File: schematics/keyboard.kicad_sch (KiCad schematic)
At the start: 35 parts

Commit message: cleanup, fixes, started on power supplies
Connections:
- net C6: no longer S?.2, S?.2, S?.2, S?.2
- net KB10: no longer S?.2, S?.2, S?.2, S?.2, S?.2, S?.2, S?.2, S?.2, S?.2
- net KB12: no longer S?.2, S?.2, S?.2, S?.2, S?.2, S?.2, S?.2
- net KB9: no longer S?.2, S?.2, S?.2, S?.2, S?.2, S?.2, S?.2
- no-connect marks 27 -> 54
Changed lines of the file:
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@@
   (no_connect (at 236.22 73.66))
   (no_connect (at 254 53.34))
+  (no_connect (at 149.86 63.5))
+  (no_connect (at 149.86 53.34))
+  (no_connect (at 132.08 53.34))
+  (no_connect (at 132.08 63.5))
+  (no_connect (at 88.9 83.82))
+  (no_connect (at 88.9 53.34))
+  (no_connect (at 88.9 63.5))
+  (no_connect (at 149.86 83.82))
+  (no_connect (at 132.08 83.82))
+  (no_connect (at 109.22 83.82))
+  (no_connect (at 109.22 63.5))
+  (no_connect (at 208.28 83.82))
+  (no_connect (at 172.72 63.5))
+  (no_connect (at 190.5 73.66))
+  (no_connect (at 190.5 63.5))
+  (no_connect (at 172.72 53.34))
+  (no_connect (at 226.06 83.82))
+  (no_connect (at 226.06 63.5))
+  (no_connect (at 226.06 73.66))
+  (no_connect (at 226.06 53.34))
+  (no_connect (at 208.28 73.66))
+  (no_connect (at 208.28 53.34))
+  (no_connect (at 208.28 63.5))
+  (no_connect (at 243.84 63.5))
+  (no_connect (at 243.84 53.34))
+  (no_connect (at 243.84 73.66))
+  (no_connect (at 243.84 83.82))
   (no_connect (at 99.06 83.82))
   (no_connect (at 218.44 63.5))
@@
     (pin "9")
   )
-  (symbol (lib_id "Custom:SW_Push_SPDT") (at 114.3 60.96 0) (unit 1)
+  (symbol (lib_name "SW_Push_SPDT_11") (lib_id "Custom:SW_Push_SPDT") (at 114.3 60.96 0) (unit 1)
     (in_bom yes) (on_board yes)
     (property "Reference" "S?" (id 0) (at 114.3 60.96 0))
@@
     (pin "4")
   )
-  (symbol (lib_id "Custom:SW_Push_SPDT") (at 213.36 71.12 0) (unit 1)
+  (symbol (lib_name "SW_Push_SPDT_26") (lib_id "Custom:SW_Push_SPDT") (at 213.36 71.12 0) (unit 1)
     (in_bom yes) (on_board yes)
     (property "Reference" "S?" (id 0) (at 213.36 71.12 0))
@@
     (pin "2")
   )
-  (symbol (lib_id "Custom:SW_Push_SPDT") (at 248.92 60.96 0) (unit 1)
+  (symbol (lib_name "SW_Push_SPDT_18") (lib_id "Custom:SW_Push_SPDT") (at 248.92 60.96 0) (unit 1)
     (in_bom yes) (on_board yes)
     (property "Reference" "S?" (id 0) (at 248.92 60.96 0))
@@
     (pin "4")
   )
-  (symbol (lib_id "Custom:SW_Push_SPDT") (at 231.14 81.28 0) (unit 1)
+  (symbol (lib_name "SW_Push_SPDT_19") (lib_id "Custom:SW_Push_SPDT") (at 231.14 81.28 0) (unit 1)
     (in_bom yes) (on_board yes)
     (property "Reference" "S?" (id 0) (at 231.14 81.28 0))
@@
     (pin "9")
   )
-  (symbol (lib_id "Custom:SW_Push_SPDT") (at 93.98 81.28 0) (unit 1)
+  (symbol (lib_name "SW_Push_SPDT_8") (lib_id "Custom:SW_Push_SPDT") (at 93.98 81.28 0) (unit 1)
     (in_bom yes) (on_board yes)
     (property "Reference" "S?" (id 0) (at 93.98 81.28 0))
@@
     (pin "4")
   )
-  (symbol (lib_id "Custom:SW_Push_SPDT") (at 231.14 60.96 0) (unit 1)
+  (symbol (lib_name "SW_Push_SPDT_22") (lib_id "Custom:SW_Push_SPDT") (at 231.14 60.96 0) (unit 1)
     (in_bom yes) (on_board yes)
     (property "Reference" "S?" (id 0) (at 231.14 60.96 0))
@@
     (pin "4")
   )
-  (symbol (lib_id "Custom:SW_Push_SPDT") (at 154.94 50.8 0) (unit 1)
+  (symbol (lib_name "SW_Push_SPDT_2") (lib_id "Custom:SW_Push_SPDT") (at 154.94 50.8 0) (unit 1)
     (in_bom yes) (on_board yes)
     (property "Reference" "S?" (id 0) (at 154.94 50.8 0))
@@
     (pin "4")
   )
-  (symbol (lib_id "Custom:SW_Push_SPDT") (at 137.16 60.96 0) (unit 1)
+  (symbol (lib_name "SW_Push_SPDT_4") (lib_id "Custom:SW_Push_SPDT") (at 137.16 60.96 0) (unit 1)
     (in_bom yes) (on_board yes)
     (property "Reference" "S?" (id 0) (at 137.16 60.96 0))
@@
     (pin "4")
   )
-  (symbol (lib_id "Custom:SW_Push_SPDT") (at 137.16 81.28 0) (unit 1)
+  (symbol (lib_name "SW_Push_SPDT_7") (lib_id "Custom:SW_Push_SPDT") (at 137.16 81.28 0) (unit 1)
     (in_bom yes) (on_board yes)
     (property "Reference" "S?" (id 0) (at 137.16 81.28 0))
@@
     (pin "4")
   )
-  (symbol (lib_id "Custom:SW_Push_SPDT") (at 177.8 60.96 0) (unit 1)
+  (symbol (lib_name "SW_Push_SPDT_14") (lib_id "Custom:SW_Push_SPDT") (at 177.8 60.96 0) (unit 1)
     (in_bom yes) (on_board yes)
     (property "Reference" "S?" (id 0) (at 177.8 60.96 0))
@@
     (pin "4")
   )
-  (symbol (lib_id "Custom:SW_Push_SPDT") (at 248.92 71.12 0) (unit 1)
+  (symbol (lib_name "SW_Push_SPDT_20") (lib_id "Custom:SW_Push_SPDT") (at 248.92 71.12 0) (unit 1)
     (in_bom yes) (on_board yes)
     (property "Reference" "S?" (id 0) (at 248.92 71.12 0))
@@
     (pin "4")
   )
-  (symbol (lib_id "Custom:SW_Push_SPDT") (at 231.14 50.8 0) (unit 1)
+  (symbol (lib_name "SW_Push_SPDT_24") (lib_id "Custom:SW_Push_SPDT") (at 231.14 50.8 0) (unit 1)
     (in_bom yes) (on_board yes)
     (property "Reference" "S?" (id 0) (at 231.14 50.8 0))
@@
     (pin "4")
   )
-  (symbol (lib_id "Custom:SW_Push_SPDT") (at 93.98 60.96 0) (unit 1)
+  (symbol (lib_name "SW_Push_SPDT_6") (lib_id "Custom:SW_Push_SPDT") (at 93.98 60.96 0) (unit 1)
     (in_bom yes) (on_board yes)
     (property "Reference" "S?" (id 0) (at 93.98 60.96 0))
@@
     (pin "4")
   )
-  (symbol (lib_id "Custom:SW_Push_SPDT") (at 177.8 50.8 0) (unit 1)
+  (symbol (lib_name "SW_Push_SPDT_16") (lib_id "Custom:SW_Push_SPDT") (at 177.8 50.8 0) (unit 1)
     (in_bom yes) (on_board yes)
     (property "Reference" "S?" (id 0) (at 177.8 50.8 0))
@@
     (pin "4")
   )
-  (symbol (lib_id "Custom:SW_Push_SPDT") (at 154.94 81.28 0) (unit 1)
+  (symbol (lib_name "SW_Push_SPDT_9") (lib_id "Custom:SW_Push_SPDT") (at 154.94 81.28 0) (unit 1)
     (in_bom yes) (on_board yes)
     (property "Reference" "S?" (id 0) (at 154.94 81.28 0))
@@
     (pin "2")
   )
-  (symbol (lib_id "Custom:SW_Push_SPDT") (at 154.94 60.96 0) (unit 1)
+  (symbol (lib_name "SW_Push_SPDT_3") (lib_id "Custom:SW_Push_SPDT") (at 154.94 60.96 0) (unit 1)
     (in_bom yes) (on_board yes)
     (property "Reference" "S?" (id 0) (at 154.94 60.96 0))
@@
     (pin "4")
   )
-  (symbol (lib_id "Custom:SW_Push_SPDT") (at 195.58 71.12 0) (unit 1)
+  (symbol (lib_name "SW_Push_SPDT_13") (lib_id "Custom:SW_Push_SPDT") (at 195.58 71.12 0) (unit 1)
     (in_bom no) (on_board yes)
     (property "Reference" "S?" (id 0) (at 195.58 71.12 0))
@@
     (pin "2")
   )
-  (symbol (lib_id "Custom:SW_Push_SPDT") (at 248.92 81.28 0) (unit 1)
+  (symbol (lib_name "SW_Push_SPDT_21") (lib_id "Custom:SW_Push_SPDT") (at 248.92 81.28 0) (unit 1)
     (in_bom yes) (on_board yes)
     (property "Reference" "S?" (id 0) (at 248.92 81.28 0))
@@
     (pin "4")
   )
-  (symbol (lib_id "Custom:SW_Push_SPDT") (at 93.98 50.8 0) (unit 1)
+  (symbol (lib_name "SW_Push_SPDT_5") (lib_id "Custom:SW_Push_SPDT") (at 93.98 50.8 0) (unit 1)
     (in_bom yes) (on_board yes)
     (property "Reference" "S?" (id 0) (at 93.98 50.8 0))
@@
     (pin "2")
   )
-  (symbol (lib_id "Custom:SW_Push_SPDT") (at 114.3 81.28 0) (unit 1)
+  (symbol (lib_name "SW_Push_SPDT_10") (lib_id "Custom:SW_Push_SPDT") (at 114.3 81.28 0) (unit 1)
     (in_bom yes) (on_board yes)
     (property "Reference" "S?" (id 0) (at 114.3 81.28 0))
@@
     (pin "4")
   )
-  (symbol (lib_id "Custom:SW_Push_SPDT") (at 213.36 60.96 0) (unit 1)
+  (symbol (lib_name "SW_Push_SPDT_25") (lib_id "Custom:SW_Push_SPDT") (at 213.36 60.96 0) (unit 1)
     (in_bom yes) (on_board yes)
     (property "Reference" "S?" (id 0) (at 213.36 60.96 0))
@@
     (pin "4")
   )
-  (symbol (lib_id "Custom:SW_Push_SPDT") (at 213.36 81.28 0) (unit 1)
+  (symbol (lib_name "SW_Push_SPDT_12") (lib_id "Custom:SW_Push_SPDT") (at 213.36 81.28 0) (unit 1)
     (in_bom yes) (on_board yes)
     (property "Reference" "S?" (id 0) (at 213.36 81.28 0))
@@
     (pin "4")
   )
-  (symbol (lib_id "Custom:SW_Push_SPDT") (at 248.92 50.8 0) (unit 1)
+  (symbol (lib_name "SW_Push_SPDT_17") (lib_id "Custom:SW_Push_SPDT") (at 248.92 50.8 0) (unit 1)
     (in_bom yes) (on_board yes)
     (property "Reference" "S?" (id 0) (at 248.92 50.8 0))
@@
     (pin "4")
   )
-  (symbol (lib_id "Custom:SW_Push_SPDT") (at 137.16 50.8 0) (unit 1)
+  (symbol (lib_name "SW_Push_SPDT_1") (lib_id "Custom:SW_Push_SPDT") (at 137.16 50.8 0) (unit 1)
     (in_bom yes) (on_board yes)
     (property "Reference" "S?" (id 0) (at 137.16 50.8 0))
@@
     (pin "4")
   )
-  (symbol (lib_id "Custom:SW_Push_SPDT") (at 231.14 71.12 0) (unit 1)
+  (symbol (lib_name "SW_Push_SPDT_23") (lib_id "Custom:SW_Push_SPDT") (at 231.14 71.12 0) (unit 1)
     (in_bom yes) (on_board yes)
     (property "Reference" "S?" (id 0) (at 231.14 71.12 0))
@@
     (pin "4")
   )
-  (symbol (lib_id "Custom:SW_Push_SPDT") (at 195.58 60.96 0) (unit 1)
+  (symbol (lib_name "SW_Push_SPDT_15") (lib_id "Custom:SW_Push_SPDT") (at 195.58 60.96 0) (unit 1)
     (in_bom yes) (on_board yes)
     (property "Reference" "S?" (id 0) (at 195.58 60.96 0))

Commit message: More power supply work
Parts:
- U?: value 74LS33 -> 74LD33

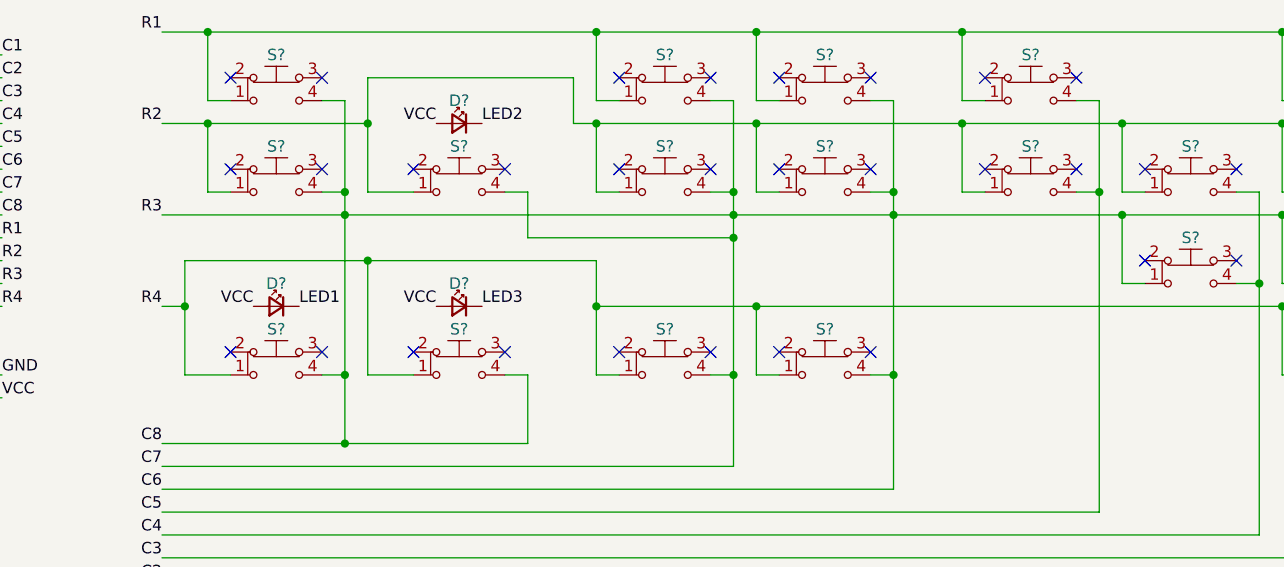
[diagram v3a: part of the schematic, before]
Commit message: Updated to KiCad v10.0. Minor improvements.
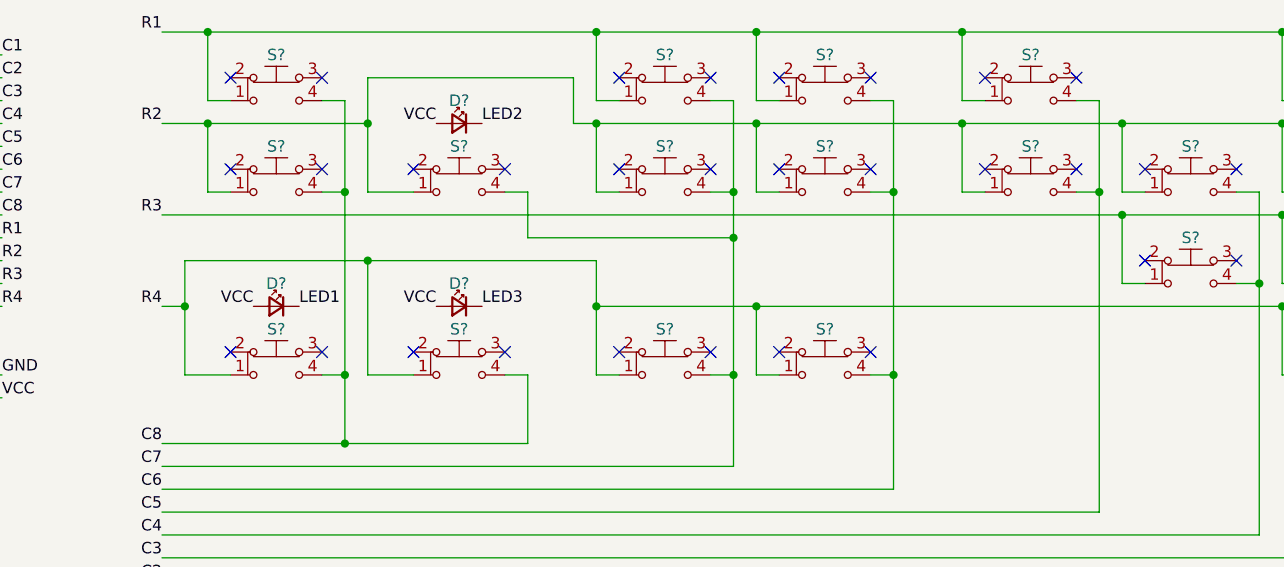
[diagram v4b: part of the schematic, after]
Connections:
- net C6: no longer J?.11 (Pin_11), J?.7 (Pin_7), J?.8 (Pin_8), S?.1, S?.1, S?.1, S?.1, S?.4, S?.4, S?.4, S?.4, S?.4, S?.4, S?.4, S?.4
- new net C7: J?.7 (Pin_7), S?.4, S?.4, S?.4, S?.4
- new net C8: J?.8 (Pin_8), S?.4, S?.4, S?.4, S?.4
- new net KB11: J?.11 (Pin_11), S?.1, S?.1, S?.1, S?.1
